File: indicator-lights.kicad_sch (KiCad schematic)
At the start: 17 parts, among them IC7 LP55231SQX_NOPB

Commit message: first round of revisions
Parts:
- removed C49 (x2): 1u, CAPC1608X90N, symbol SamacSys_Parts:0603YD105KAT2A
- removed C61, C62: .47u, CAPC0603X33N, symbol SamacSys_Parts:LMK063BC6474KPLF
- removed IC7: LP55231SQX_NOPB, SamacSys_Parts:QFN50P400X400X80-25N, symbol SamacSys_Parts:LP55231SQX_NOPB
- removed LED3, LED4, LED5: 150505M173300, 150505M173300, symbol SamacSys_Parts:150505M173300
- removed R15 (x3): 470R, RESC2012X60N, symbol SamacSys_Parts:AC0805FR-07470RL
- removed R45, R48, R51: 3.3k, RESC1608X55N, symbol SamacSys_Parts:RC0603JR-133K3L
- removed R? (x3): 1K, SamacSys_Parts:RESC2012X60N, symbol SamacSys_Parts:SG73P2ATTD102J
- added C16: 0.1u, SamacSys_Parts:CAPC0402X22N, symbol SamacSys_Parts:01016D104KAT2A
- added C20: 1u, SamacSys_Parts:CAPC1608X90N, symbol SamacSys_Parts:0603YD105KAT2A
- added IC7: IS31FL3218-GRLS2, SOIC127P1036X265-24N, symbol SamacSys_Parts:IS31FL3218-GRLS2
- added LED1 (x3): 150120M173000, 150120M173000, symbol SamacSys_Parts:150120M173000
- added R44: 3.3k, RESC1608X55N, symbol SamacSys_Parts:RC0603JR-133K3L
- added R?: 1K, SamacSys_Parts:RESC2012X60N, symbol SamacSys_Parts:SG73P2ATTD102J
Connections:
- net +3V3: now also C16.1, C20.2, IC7.3 (VCC), LED1.2 (A_G), LED1.2 (A_G), LED1.2 (A_G), R?.2
- net GND: now also C16.2, C20.1, IC7.4 (GND), R44.1
- net SCL: now also IC7.6 (SCL)
- net SDA: now also IC7.5 (SDA)
- new net: IC7.2 (R_EXT), R44.2
- new net: IC7.24 (~{SDB}), R?.1
- new net O1: IC7.7 (O1)
- new net O10: IC7.16 (O10), LED1.3 (K_G)
- new net O11: IC7.17 (O11), LED1.4 (K_R)
- new net O12: IC7.18 (O12), LED1.1 (K_B)
- new net O13: IC7.19 (O13), LED1.3 (K_G)
- new net O14: IC7.20 (O14), LED1.4 (K_R)
- new net O15: IC7.21 (O15), LED1.1 (K_B)
- new net O16: IC7.22 (O16)
- new net O17: IC7.23 (O17)
- new net O18: IC7.1 (O18)
- new net O2: IC7.8 (O2)
- new net O3: IC7.9 (O3)
- new net O4: IC7.10 (O4)
- new net O5: IC7.11 (O5)
- new net O6: IC7.12 (O6)
- new net O7: IC7.13 (O7), LED1.3 (K_G)
- new net O8: IC7.14 (O8), LED1.4 (K_R)
- new net O9: IC7.15 (O9), LED1.1 (K_B)
- no-connect marks 0 -> 9
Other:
- note removed: "I2C ADDR 32H (8-bit: W:64H / R:65H) WHEN ASEL0/1 PULLED TO GND"
- note removed: "TODO: Replace with IS31FL3218 as well as a common-anode LED array (use the ones from the original design, they're good). This IC is pinless and a PITA."

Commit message: fully move to new MCU configuration
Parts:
- removed R?: 1K, SamacSys_Parts:RESC2012X60N, symbol SamacSys_Parts:SG73P2ATTD102J
- added R10: 10k, SamacSys_Parts:RESC5025X65N, symbol SamacSys_Parts:RC2010JK-0710KL
- renumbered R44 to R34
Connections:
- net +3V3: now also R10.1
- net at IC7.24 (~{SDB}): now also R10.2
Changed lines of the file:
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@@
         )
         (path "/e89dcd22-1250-4a5b-b778-1c95a0dd623d/49c51f54-e113-47ff-b1ad-86c9ad73cafa"
-          (reference "C61") (unit 1)
+          (reference "C62") (unit 1)
         )
       )
@@
   (symbol (lib_id "power:+3V3") (at 149.86 73.66 0) (unit 1)
     (in_bom yes) (on_board yes) (dnp no) (fields_autoplaced)
-    (property "Reference" "#PWR0126" (at 149.86 77.47 0)
+    (property "Reference" "#PWR0119" (at 149.86 77.47 0)
       (effects (font (size 1.27 1.27)) hide)
     )
@@
       (project "Oro Link rev2"
         (path "/e89dcd22-1250-4a5b-b778-1c95a0dd623d/49c51f54-e113-47ff-b1ad-86c9ad73cafa"
-          (reference "#PWR0126") (unit 1)
+          (reference "#PWR0119") (unit 1)
         )
       )
@@
   (symbol (lib_id "SamacSys_Parts:RC0603JR-133K3L") (at 85.09 109.22 0) (unit 1)
     (in_bom yes) (on_board yes) (dnp no)
-    (property "Reference" "R44" (at 87.63 110.49 0)
+    (property "Reference" "R34" (at 87.63 110.49 0)
       (effects (font (size 1.27 1.27)))
     )
@@
       (project "Oro Link rev2"
         (path "/e89dcd22-1250-4a5b-b778-1c95a0dd623d/49c51f54-e113-47ff-b1ad-86c9ad73cafa"
-          (reference "R44") (unit 1)
+          (reference "R34") (unit 1)
         )
       )
@@
         )
         (path "/e89dcd22-1250-4a5b-b778-1c95a0dd623d/49c51f54-e113-47ff-b1ad-86c9ad73cafa"
-          (reference "C60") (unit 1)
+          (reference "C61") (unit 1)
         )
       )
@@
   (symbol (lib_id "power:GND") (at 83.82 113.03 0) (unit 1)
     (in_bom yes) (on_board yes) (dnp no) (fields_autoplaced)
-    (property "Reference" "#PWR0125" (at 83.82 119.38 0)
+    (property "Reference" "#PWR0118" (at 83.82 119.38 0)
       (effects (font (size 1.27 1.27)) hide)
     )
@@
       (project "Oro Link rev2"
         (path "/e89dcd22-1250-4a5b-b778-1c95a0dd623d/49c51f54-e113-47ff-b1ad-86c9ad73cafa"
-          (reference "#PWR0125") (unit 1)
+          (reference "#PWR0118") (unit 1)
         )
       )
@@
   (symbol (lib_id "power:+3V3") (at 83.82 91.44 0) (unit 1)
     (in_bom yes) (on_board yes) (dnp no) (fields_autoplaced)
-    (property "Reference" "#PWR0124" (at 83.82 95.25 0)
+    (property "Reference" "#PWR0117" (at 83.82 95.25 0)
       (effects (font (size 1.27 1.27)) hide)
     )
@@
       (project "Oro Link rev2"
         (path "/e89dcd22-1250-4a5b-b778-1c95a0dd623d/49c51f54-e113-47ff-b1ad-86c9ad73cafa"
-          (reference "#PWR0124") (unit 1)
+          (reference "#PWR0117") (unit 1)
         )
       )
@@
     )
   )
-  (symbol (lib_id "SamacSys_Parts:SG73P2ATTD102J") (at 149.86 93.98 90) (unit 1)
-    (in_bom yes) (on_board yes) (dnp no) (fields_autoplaced)
-    (property "Reference" "R?" (at 151.8412 84.4463 90)
+  (symbol (lib_id "SamacSys_Parts:RC2010JK-0710KL") (at 149.86 76.2 270) (unit 1)
+    (in_bom yes) (on_board yes) (dnp no)
+    (property "Reference" "R10" (at 156.21 83.82 90)
       (effects (font (size 1.27 1.27)) (justify right))
     )
-    (property "Value" "1K" (at 151.8412 86.3673 90)
+    (property "Value" "10k" (at 156.21 86.36 90)
       (effects (font (size 1.27 1.27)) (justify right))
     )
-    (property "Footprint" "SamacSys_Parts:RESC2012X60N" (at 148.59 80.01 0)
-      (effects (font (size 1.27 1.27)) (justify left) hide)
-    )
-    (property "Datasheet" "https://componentsearchengine.com/Datasheets/1/SG73P2ATTD102J.pdf" (at 151.13 80.01 0)
-      (effects (font (size 1.27 1.27)) (justify left) hide)
-    )
-    (property "Description" "Thick Film Resistors - SMD 0.25W 1Kohm 5% 200ppm Anti-Pulse" (at 153.67 80.01 0)
-      (effects (font (size 1.27 1.27)) (justify left) hide)
-    )
-    (property "Height" "0.6" (at 156.21 80.01 0)
-      (effects (font (size 1.27 1.27)) (justify left) hide)
-    )
-    (property "Manufacturer_Name" "KOA Speer" (at 158.75 80.01 0)
-      (effects (font (size 1.27 1.27)) (justify left) hide)
-    )
-    (property "Manufacturer_Part_Number" "SG73P2ATTD102J" (at 161.29 80.01 0)
-      (effects (font (size 1.27 1.27)) (justify left) hide)
-    )
-    (property "Mouser Part Number" "660-SG73P2ATTD102J" (at 163.83 80.01 0)
-      (effects (font (size 1.27 1.27)) (justify left) hide)
-    )
-    (property "Mouser Price/Stock" "https://www.mouser.com/Search/Refine.aspx?Keyword=660-SG73P2ATTD102J" (at 166.37 80.01 0)
-      (effects (font (size 1.27 1.27)) (justify left) hide)
-    )
-    (property "Arrow Part Number" "CRGP2512F1K0" (at 168.91 80.01 0)
-      (effects (font (size 1.27 1.27)) (justify left) hide)
-    )
-    (property "Arrow Price/Stock" "https://www.arrow.com/en/products/crgp2512f1k0/te-connectivity" (at 171.45 80.01 0)
-      (effects (font (size 1.27 1.27)) (justify left) hide)
-    )
-    (property "Mouser Testing Part Number" "" (at 173.99 80.01 0)
-      (effects (font (size 1.27 1.27)) (justify left) hide)
-    )
-    (property "Mouser Testing Price/Stock" "" (at 176.53 80.01 0)
+    (property "Footprint" "SamacSys_Parts:RESC5025X65N" (at 151.13 90.17 0)
+      (effects (font (size 1.27 1.27)) (justify left) hide)
+    )
+    (property "Datasheet" "https://www.arrow.com/en/products/rc2010jk-0710kl/yageo" (at 148.59 90.17 0)
+      (effects (font (size 1.27 1.27)) (justify left) hide)
+    )
+    (property "Description" "Res Thick Film 2010 10K Ohm 5% 0.75W(3/4W) +/-100ppm/C Pad SMD T/R" (at 146.05 90.17 0)
+      (effects (font (size 1.27 1.27)) (justify left) hide)
+    )
+    (property "Height" "0.65" (at 143.51 90.17 0)
+      (effects (font (size 1.27 1.27)) (justify left) hide)
+    )
+    (property "Manufacturer_Name" "KEMET" (at 140.97 90.17 0)
+      (effects (font (size 1.27 1.27)) (justify left) hide)
+    )
+    (property "Manufacturer_Part_Number" "RC2010JK-0710KL" (at 138.43 90.17 0)
+      (effects (font (size 1.27 1.27)) (justify left) hide)
+    )
+    (property "Mouser Part Number" "603-RC2010JK-0710KL" (at 135.89 90.17 0)
+      (effects (font (size 1.27 1.27)) (justify left) hide)
+    )
+    (property "Mouser Price/Stock" "https://www.mouser.co.uk/ProductDetail/YAGEO/RC2010JK-0710KL?qs=sNpmnPgvziOLj5uuquGIow%3D%3D" (at 133.35 90.17 0)
+      (effects (font (size 1.27 1.27)) (justify left) hide)
+    )
+    (property "Arrow Part Number" "RC2010JK-0710KL" (at 130.81 90.17 0)
+      (effects (font (size 1.27 1.27)) (justify left) hide)
+    )
+    (property "Arrow Price/Stock" "https://www.arrow.com/en/products/rc2010jk-0710kl/yageo" (at 128.27 90.17 0)
+      (effects (font (size 1.27 1.27)) (justify left) hide)
+    )
+    (property "Mouser Testing Part Number" "" (at 125.73 90.17 0)
+      (effects (font (size 1.27 1.27)) (justify left) hide)
+    )
+    (property "Mouser Testing Price/Stock" "" (at 123.19 90.17 0)
       (effects (font (size 1.27 1.27)) (justify left) hide)
     )
@@
       (project "Oro Testbed v2"
         (path "/3d0fc623-63eb-45e5-a304-e470d9b3a173"
-          (reference "R?") (unit 1)
-        )
-        (path "/3d0fc623-63eb-45e5-a304-e470d9b3a173/62e8cddc-1c26-4fab-8954-689e69f767da"
-          (reference "R13") (unit 1)
-        )
-      )
-      (project "Oro Link rev2"
-        (path "/e89dcd22-1250-4a5b-b778-1c95a0dd623d/f955395e-bf1a-4ef3-9cfe-ec9d49f66988"
-          (reference "R1") (unit 1)
-        )
-        (path "/e89dcd22-1250-4a5b-b778-1c95a0dd623d/49c51f54-e113-47ff-b1ad-86c9ad73cafa"
-          (reference "R45") (unit 1)
+          (reference "R10") (unit 1)
+        )
+        (path "/3d0fc623-63eb-45e5-a304-e470d9b3a173/7310340d-2c15-4c32-b17d-f4923dae9f8e"
+          (reference "R8") (unit 1)
+        )
+      )
+      (project "Oro Link rev2"
+        (path "/e89dcd22-1250-4a5b-b778-1c95a0dd623d/1b3eede1-74b0-4c0b-b4f1-7ec1bfc1f54f"
+          (reference "R16") (unit 1)
+        )
+        (path "/e89dcd22-1250-4a5b-b778-1c95a0dd623d/52771c01-2e58-4900-abe5-411f688d020f"
+          (reference "R8") (unit 1)
+        )
+        (path "/e89dcd22-1250-4a5b-b778-1c95a0dd623d/7cebe953-3148-4b67-a6c9-1f2594261687"
+          (reference "R20") (unit 1)
+        )
+        (path "/e89dcd22-1250-4a5b-b778-1c95a0dd623d/dd173832-34f8-47c0-be66-f527d6e2d134"
+          (reference "R3") (unit 1)
+        )
+        (path "/e89dcd22-1250-4a5b-b778-1c95a0dd623d/49c51f54-e113-47ff-b1ad-86c9ad73cafa"
+          (reference "R35") (unit 1)
         )
       )
@@
   (symbol (lib_id "power:+3V3") (at 167.64 73.66 0) (unit 1)
     (in_bom yes) (on_board yes) (dnp no) (fields_autoplaced)
-    (property "Reference" "#PWR0127" (at 167.64 77.47 0)
+    (property "Reference" "#PWR0120" (at 167.64 77.47 0)
       (effects (font (size 1.27 1.27)) hide)
     )
@@
       (project "Oro Link rev2"
         (path "/e89dcd22-1250-4a5b-b778-1c95a0dd623d/49c51f54-e113-47ff-b1ad-86c9ad73cafa"
-          (reference "#PWR0127") (unit 1)
-        )
-      )
+          (reference "#PWR0120") (unit 1)
+        )
+      )

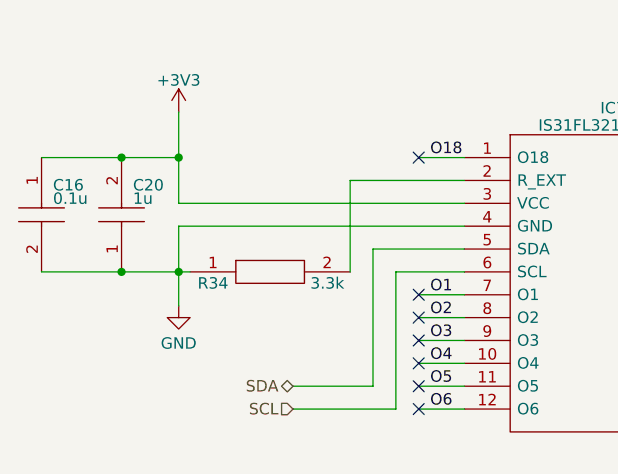
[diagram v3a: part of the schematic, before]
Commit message: first few boards laid out
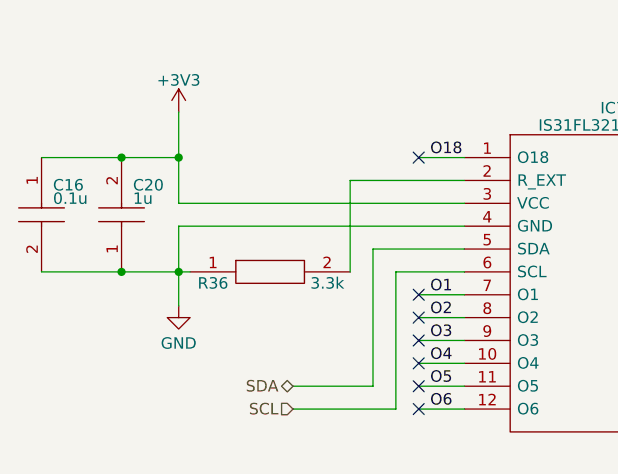
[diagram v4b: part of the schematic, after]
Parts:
- renumbered R34 to R36
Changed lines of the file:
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@@
     (rev "2")
     (company "Oro Operating System")
+    (comment 1 "://oro.sh")
+    (comment 2 "Joshua Lee Junon")
   )
   (junction (at 77.47 96.52) (diameter 0) (color 0 0 0 0)
@@
         )
         (path "/e89dcd22-1250-4a5b-b778-1c95a0dd623d/49c51f54-e113-47ff-b1ad-86c9ad73cafa"
-          (reference "C62") (unit 1)
+          (reference "C61") (unit 1)
         )
       )
@@
   (symbol (lib_id "power:+3V3") (at 149.86 73.66 0) (unit 1)
     (in_bom yes) (on_board yes) (dnp no) (fields_autoplaced)
-    (property "Reference" "#PWR0119" (at 149.86 77.47 0)
+    (property "Reference" "#PWR0149" (at 149.86 77.47 0)
       (effects (font (size 1.27 1.27)) hide)
     )
@@
       (project "Oro Link rev2"
         (path "/e89dcd22-1250-4a5b-b778-1c95a0dd623d/49c51f54-e113-47ff-b1ad-86c9ad73cafa"
-          (reference "#PWR0119") (unit 1)
+          (reference "#PWR0149") (unit 1)
         )
       )
@@
   (symbol (lib_id "SamacSys_Parts:RC0603JR-133K3L") (at 85.09 109.22 0) (unit 1)
     (in_bom yes) (on_board yes) (dnp no)
-    (property "Reference" "R34" (at 87.63 110.49 0)
+    (property "Reference" "R36" (at 87.63 110.49 0)
       (effects (font (size 1.27 1.27)))
     )
@@
       (project "Oro Link rev2"
         (path "/e89dcd22-1250-4a5b-b778-1c95a0dd623d/49c51f54-e113-47ff-b1ad-86c9ad73cafa"
-          (reference "R34") (unit 1)
+          (reference "R36") (unit 1)
         )
       )
@@
       (project "Oro Link rev2"
         (path "/e89dcd22-1250-4a5b-b778-1c95a0dd623d/49c51f54-e113-47ff-b1ad-86c9ad73cafa"
-          (reference "LED4") (unit 1)
+          (reference "LED5") (unit 1)
         )
       )
@@
       (project "Oro Link rev2"
         (path "/e89dcd22-1250-4a5b-b778-1c95a0dd623d/49c51f54-e113-47ff-b1ad-86c9ad73cafa"
-          (reference "LED5") (unit 1)
+          (reference "LED6") (unit 1)
         )
       )
@@
         )
         (path "/e89dcd22-1250-4a5b-b778-1c95a0dd623d/49c51f54-e113-47ff-b1ad-86c9ad73cafa"
-          (reference "C61") (unit 1)
+          (reference "C60") (unit 1)
         )
       )
@@
   (symbol (lib_id "power:GND") (at 83.82 113.03 0) (unit 1)
     (in_bom yes) (on_board yes) (dnp no) (fields_autoplaced)
-    (property "Reference" "#PWR0118" (at 83.82 119.38 0)
+    (property "Reference" "#PWR0148" (at 83.82 119.38 0)
       (effects (font (size 1.27 1.27)) hide)
     )
@@
       (project "Oro Link rev2"
         (path "/e89dcd22-1250-4a5b-b778-1c95a0dd623d/49c51f54-e113-47ff-b1ad-86c9ad73cafa"
-          (reference "#PWR0118") (unit 1)
+          (reference "#PWR0148") (unit 1)
         )
       )
@@
   (symbol (lib_id "power:+3V3") (at 83.82 91.44 0) (unit 1)
     (in_bom yes) (on_board yes) (dnp no) (fields_autoplaced)
-    (property "Reference" "#PWR0117" (at 83.82 95.25 0)
+    (property "Reference" "#PWR0147" (at 83.82 95.25 0)
       (effects (font (size 1.27 1.27)) hide)
     )
@@
       (project "Oro Link rev2"
         (path "/e89dcd22-1250-4a5b-b778-1c95a0dd623d/49c51f54-e113-47ff-b1ad-86c9ad73cafa"
-          (reference "#PWR0117") (unit 1)
+          (reference "#PWR0147") (unit 1)
         )
       )
@@
         )
         (path "/e89dcd22-1250-4a5b-b778-1c95a0dd623d/49c51f54-e113-47ff-b1ad-86c9ad73cafa"
-          (reference "R35") (unit 1)
+          (reference "R37") (unit 1)
         )
       )
@@
   (symbol (lib_id "power:+3V3") (at 167.64 73.66 0) (unit 1)
     (in_bom yes) (on_board yes) (dnp no) (fields_autoplaced)
-    (property "Reference" "#PWR0120" (at 167.64 77.47 0)
+    (property "Reference" "#PWR0150" (at 167.64 77.47 0)
       (effects (font (size 1.27 1.27)) hide)
     )
@@
       (project "Oro Link rev2"
         (path "/e89dcd22-1250-4a5b-b778-1c95a0dd623d/49c51f54-e113-47ff-b1ad-86c9ad73cafa"
-          (reference "#PWR0120") (unit 1)
+          (reference "#PWR0150") (unit 1)
         )
       )
@@
       (project "Oro Link rev2"
         (path "/e89dcd22-1250-4a5b-b778-1c95a0dd623d/49c51f54-e113-47ff-b1ad-86c9ad73cafa"
-          (reference "LED3") (unit 1)
-        )
-      )
+          (reference "LED4") (unit 1)
+        )
+      )

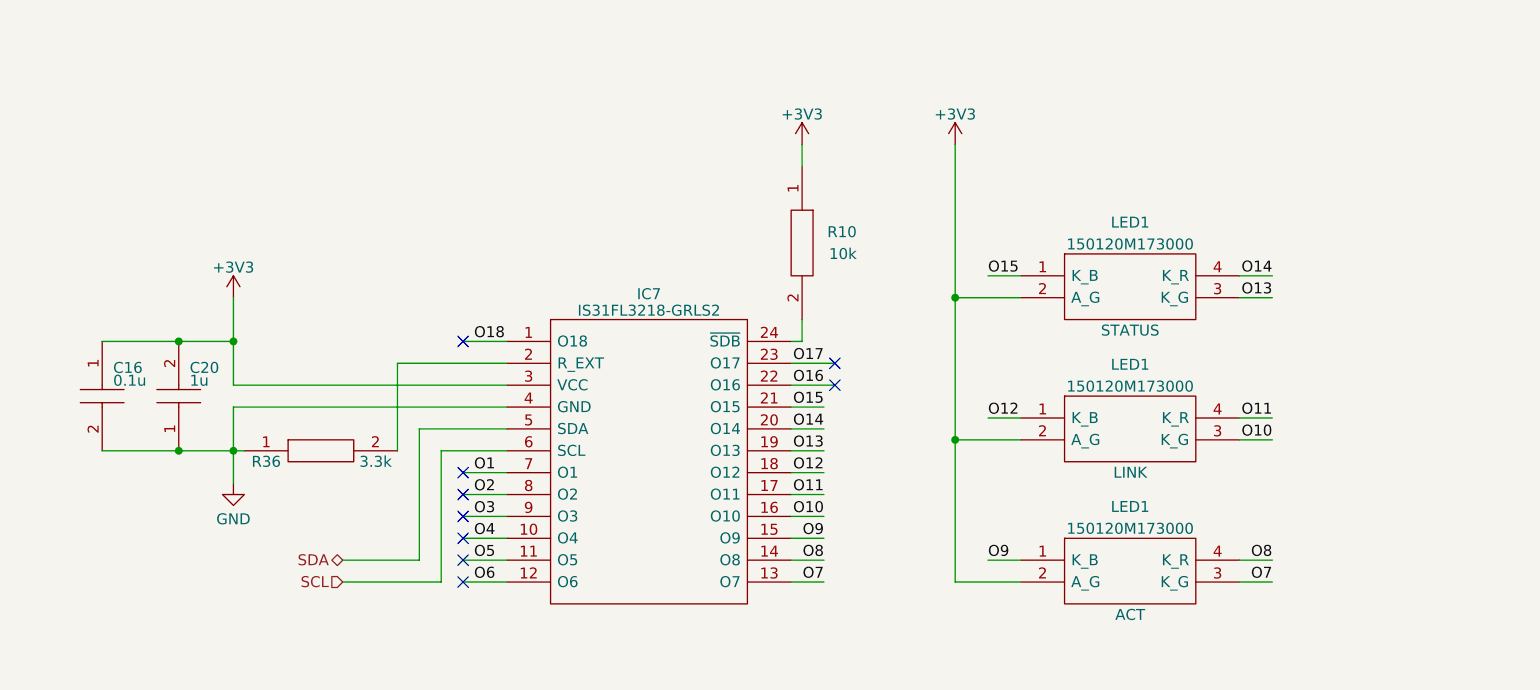
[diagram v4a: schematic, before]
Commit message: first panelization of entire modular dev board
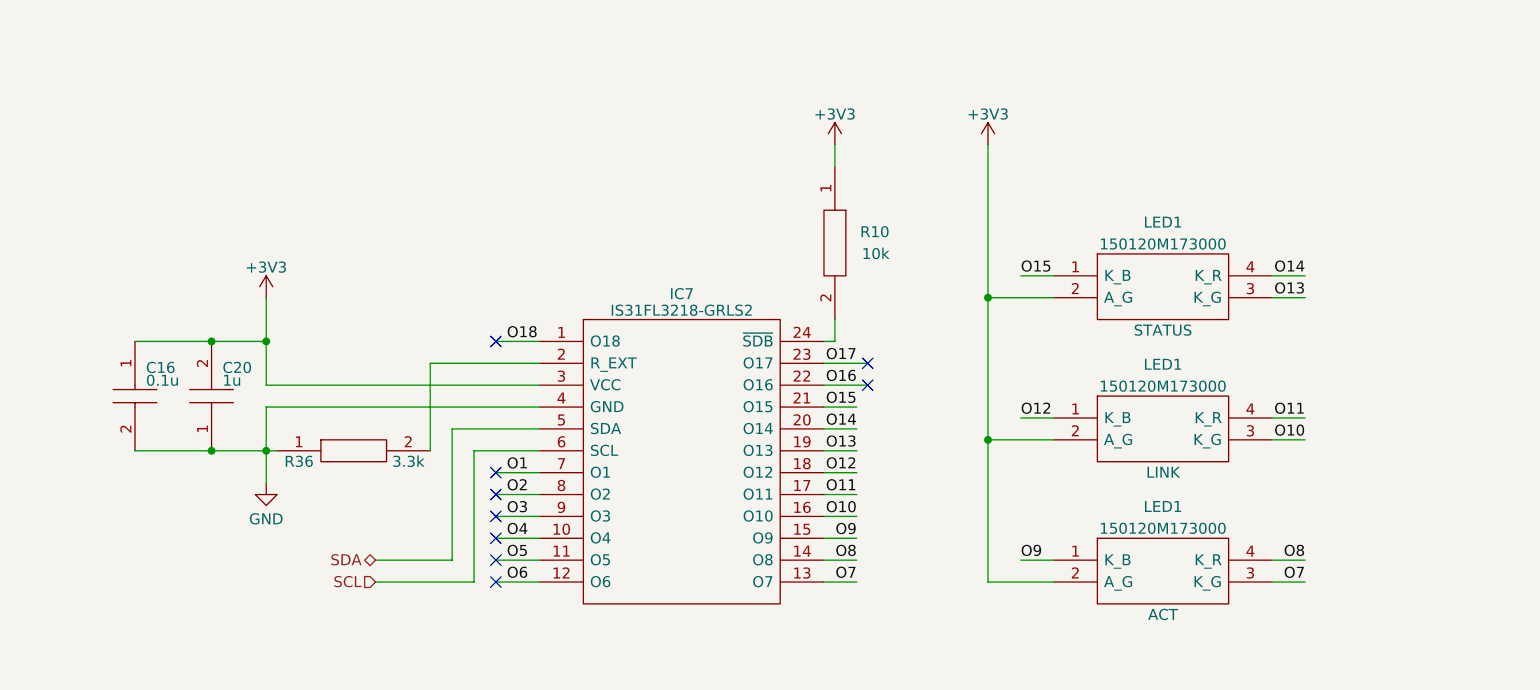
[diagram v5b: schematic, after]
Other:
- moved on the sheet: C16, C20, IC7, LED1, R10, R36
